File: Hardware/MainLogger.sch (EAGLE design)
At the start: 152 parts, among them J2 GEMS_POWER_PLUGINPUT, J3 CONN_TALON_LOGGER, J4 U.FL, J5 CONN_TALON_LOGGER, J6 CONN_TALON_LOGGER, J8 CONN_TALON_LOGGER, Q1 DMG3404, Q2 MOSFET_PCH-DMP3036SFG, Q3 MOSFET_PCH-DMP3036SFG, Q4 DMG3404, Q5 NX2301P, U1 MMC5633, U10 MXC6655, U11 FXMAR2102UMLP, U12 MCP79412SOIC, U13 SN74LVC1G17DCK, U14 TPL5010DDC, U15 MIC842L, U16 TPL5010DDC, U17 TPL5010DDC, U18 HALL_EFFECT_SI7201, U19 LP59073.3VYKE, U2 PAC1934QFN, U21 MIC22602, U3 LTC4412S6, U4 BQ25616, U5 TPS78218DBV, U6 MAX-M8W, U7 B_SERIES_M.2EKEY_3042, U8 TCR2LE31ESV, U9 TPS61282D

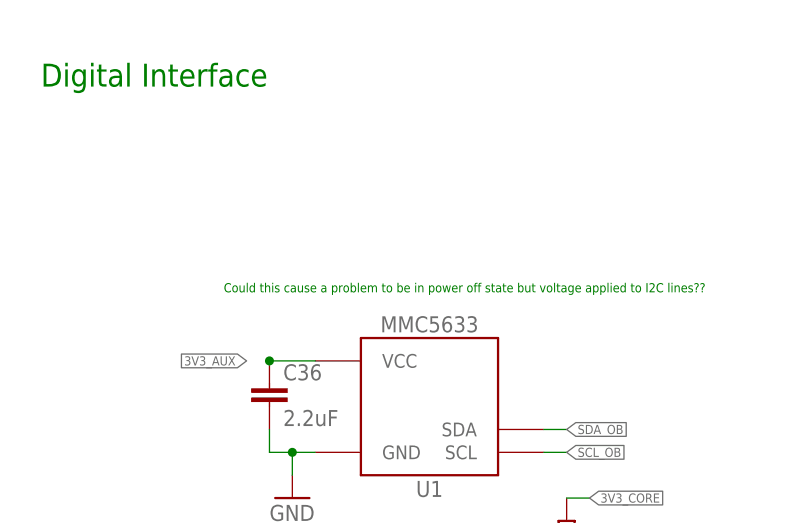
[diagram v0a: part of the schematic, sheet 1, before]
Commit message: Added VELM3328
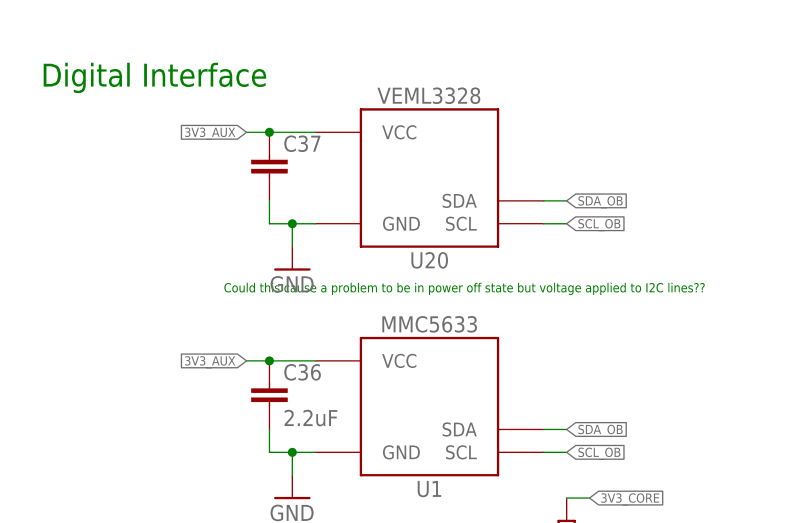
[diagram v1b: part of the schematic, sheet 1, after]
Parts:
- added C37: (no value), bschulz_passives:C-EU0.1UFC0402
- added U20: VEML3328, bschulz:VEML3328
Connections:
- net 3V3_AUX: now also C37.1, U20.VCC
- net GND: now also C37.2, U20.GND
- net SCL_OB: now also U20.SCL
- net SDA_OB: now also U20.SDA
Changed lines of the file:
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@@
 <part name="C36" library="bschulz_passives" deviceset="C-EU" device="C0603" technology="2.2UF" value="2.2uF"/>
 <part name="R6" library="bschulz_passives" deviceset="R-EU_" device="R0402" technology="10K" value="10k"/>
+<part name="U20" library="bschulz" deviceset="VEML3328" device=""/>
+<part name="GND41" library="supply1" library_urn="urn:adsk.eagle:library:371" deviceset="GND" device=""/>
+<part name="C37" library="bschulz_passives" deviceset="C-EU" device="C0402" technology="0.1UF"/>
 </parts>
 <sheets>
@@
 <attribute name="VALUE" x="69.342" y="148.59" size="1.778" layer="96" rot="R90"/>
 </instance>
+<instance part="U20" gate="G$1" x="50.8" y="193.04" smashed="yes">
+<attribute name="DISP" x="50.8" y="202.184" size="1.778" layer="95" ratio="15" align="center"/>
+<attribute name="NAME" x="50.8" y="183.896" size="1.778" layer="95" ratio="15" align="center"/>
+</instance>
+<instance part="GND41" gate="1" x="35.56" y="182.88" smashed="yes">
+<attribute name="VALUE" x="33.02" y="180.34" size="1.778" layer="96"/>
+</instance>
+<instance part="C37" gate="G$1" x="33.02" y="195.58" smashed="yes">
+<attribute name="NAME" x="34.544" y="195.961" size="1.778" layer="95"/>
+<attribute name="VALUE" x="34.544" y="190.881" size="1.778" layer="96"/>
+</instance>
 </instances>
 <busses>
@@
 <wire x1="33.02" y1="137.16" x2="35.56" y2="137.16" width="0.1524" layer="91"/>
 <junction x="35.56" y="137.16"/>
+</segment>
+<segment>
+<pinref part="U20" gate="G$1" pin="GND"/>
+<wire x1="38.1" y1="187.96" x2="35.56" y2="187.96" width="0.1524" layer="91"/>
+<wire x1="35.56" y1="187.96" x2="35.56" y2="185.42" width="0.1524" layer="91"/>
+<pinref part="GND41" gate="1" pin="GND"/>
+<pinref part="C37" gate="G$1" pin="2"/>
+<wire x1="33.02" y1="190.5" x2="33.02" y2="187.96" width="0.1524" layer="91"/>
+<wire x1="33.02" y1="187.96" x2="35.56" y2="187.96" width="0.1524" layer="91"/>
+<junction x="35.56" y="187.96"/>
 </segment>
 </net>
@@
 <label x="63.5" y="119.38" size="1.016" layer="95" xref="yes"/>
 </segment>
+<segment>
+<pinref part="U20" gate="G$1" pin="SDA"/>
+<wire x1="63.5" y1="190.5" x2="66.04" y2="190.5" width="0.1524" layer="91"/>
+<label x="66.04" y="190.5" size="1.016" layer="95" xref="yes"/>
+</segment>
 </net>
 <net name="SCL_OB" class="0">
@@
 <wire x1="63.5" y1="116.84" x2="60.96" y2="116.84" width="0.1524" layer="91"/>
 <label x="63.5" y="116.84" size="1.016" layer="95" xref="yes"/>
+</segment>
+<segment>
+<pinref part="U20" gate="G$1" pin="SCL"/>
+<wire x1="63.5" y1="187.96" x2="66.04" y2="187.96" width="0.1524" layer="91"/>
+<label x="66.04" y="187.96" size="1.016" layer="95" xref="yes"/>
 </segment>
 </net>
@@
 <pinref part="C36" gate="G$1" pin="1"/>
 <junction x="33.02" y="172.72"/>
-</segment>
-</net>
+<wire x1="33.02" y1="172.72" x2="30.48" y2="172.72" width="0.1524" layer="91"/>
+</segment>
+<segment>
+<pinref part="U20" gate="G$1" pin="VCC"/>
+<wire x1="38.1" y1="198.12" x2="33.02" y2="198.12" width="0.1524" layer="91"/>
+<pinref part="C37" gate="G$1" pin="1"/>
+<wire x1="33.02" y1="198.12" x2="30.48" y2="198.12" width="0.1524" layer="91"/>
+<junction x="33.02" y="198.12"/>
+<label x="30.48" y="198.12" size="1.016" layer="95" rot="R180" xref="yes"/>
+</segment>
+</net>

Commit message: Continued layout and schematic updates
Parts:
- removed C12: 1uF, bschulz_passives:C-EU1UFC0603
- removed C22, C30, C31: 0.1uF, bschulz_passives:C-EU0.1UFC0402
- removed C29: 10uF, bschulz_passives:C-EU10UFC0805
- removed D7: LEDRED0603, bschulz:LEDRED0603
- removed D8: LEDGREEN0603, bschulz:LEDGREEN0603
- removed FB6: (no value), bschulz:FERRITE_BEAD1KS0402
- removed J3, J5, J6, J8: CONN_TALON_LOGGER, GEMS_Plugs:CONN_TALON_LOGGER
- removed J7: (no value), bschulz:CONN_02-JST-2MM-SMT
- removed R2, R39, R4, R40, R41, R49: 10k, bschulz_passives:R-EU_10KR0402
- removed R22: 100k, bschulz_passives:R-EU_100KR0402
- removed R35: 1k, bschulz_passives:R-EU_1KR0402
- removed R36: 1k, bschulz_passives:R-EU_1KR0603
- removed R42, R43: 4.7k, bschulz_passives:R-EU_4.7KR0603
- removed S1: SP3TCS-4-13NA, bschulz:SP3TCS-4-13NA
- added C38, C41, C42, C43, C54: 0.1uF, bschulz_passives:C-EU0.1UFC0402
- added C39: 1uF, bschulz_passives:C-EU1UFC0603
- added C40: 0.1uF, bschulz_passives:C-EU0.1UFC0603
- added D1: CLVBA-FKA, bschulz:CLVBA-FKA
- added D10, D12, D13, D14, D15, D16, D17: LED0603, bschulz:LED0603
- added FB3: (no value), bschulz:FERRITE_BEAD1KS0402
- added H1, H2, H3, H4: (no value), bschulz:MOUNTING_HOLE4_NP
- added J9: (no value), bschulz:CONN_02-JST-2MM-SMT
- added R10, R52: 10k, bschulz_passives:R-EU_10KR0402
- added R51, R71, R72, R73, R74, R75, R76: 220R, bschulz_passives:R-EU_220R0603
- added R54: 100k, bschulz_passives:R-EU_100KR0603
- added R60: 0R, bschulz_passives:R-EU_0.0R0402
- added R63, R64, R65: 2m, bschulz_passives:R-EU_0.002R0805
- added R66: 10m, bschulz_passives:R-EU_0.01R0805
- added R67, R68, R69, R70: (no value), bschulz_passives:R-EU_R0603
- added R7, R8, R9: 4.7k, bschulz_passives:R-EU_4.7KR0603
- added S3, S4: BUTTON4.2X3.2, bschulz:BUTTON4.2X3.2
- added SD2: MICROSDMOLEX_503182, bschulz:MICROSDMOLEX_503182
- added U23: MB85RC, bschulz:MB85RC
- added U24: SN74AUP3G34DCU, bschulz:SN74AUP3G34DCU
- added U25: SIP32431TDFN, bschulz:SIP32431TDFN
- added U26: PAC1934QFN, bschulz:PAC1934QFN
- added U27: MCP23018QFN, bschulz:MCP23018QFN
- added U28: PCA9634QFN, bschulz:PCA9634QFN
- C11: value 1uF -> 0.1uF; device bschulz_passives:C-EU1UFC0603 -> bschulz_passives:C-EU0.1UFC0402
- C23, C24: value 6pF -> 9pF; device bschulz_passives:C-EU6PFC0402 -> bschulz_passives:C-EU9PFC0402
- C37: value (none) -> 0.1uF
- D5: value (none) -> LED0603; device bschulz:DIODE_CCBAT54CSOT23 -> bschulz:LED0603
- R1, R23, R3: value 100k -> 1M; device bschulz_passives:R-EU_100KR0402 -> bschulz_passives:R-EU_1MR0402
- R20: value 0R -> 100k; device bschulz_passives:R-EU_0.0R0402 -> bschulz_passives:R-EU_100KR0603
- R32: value 10k -> 100k; device bschulz_passives:R-EU_10KR0402 -> bschulz_passives:R-EU_100KR0402
- R33: value 10k -> 220R; device bschulz_passives:R-EU_10KR0402 -> bschulz_passives:R-EU_220R0603
- U14: value TPL5010DDC -> FXMAR2102UMLP; device bschulz:TPL5010DDC -> bschulz:FXMAR2102UMLP
- U15: value MIC842L -> SN74AUP1G08DCK; device bschulz:MIC842L -> bschulz:SN74AUP1G08DCK
- U5: value TPS78218DBV -> MCP23018QFN; device bschulz:TPS78218DBV -> bschulz:MCP23018QFN
- XTAL1: value CRYSTAL3.2X1.5 -> CRYSTAL32.768KHZ_9PF3.2X1.5; device bschulz:CRYSTAL3.2X1.5 -> bschulz:CRYSTAL32.768KHZ_9PF3.2X1.5
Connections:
- removed net !PG: D4.CATHODE, R29.1, R35.2, U4.!PG
- removed net 3V3_EXT_FAULT: D7.CATHODE
- removed net ALERT: R3.1, U2.SLOW/!ALERT
- removed net BYPASS: U9.!BYP
- removed net N$11: R22.1, S1.J3
- removed net N$14: R40.2, U14.DELAY
- removed net N$16: C29.1, R41.2, U15.INP
- removed net N$19: R39.1, R41.1, U14.RSTN
- removed net N$26: R42.2, R43.2, U15.OUT
- removed net N$27: D7.ANODE, R42.1
- removed net N$28: D8.ANODE, R43.1
- removed net N$31: R35.1
- removed net N$34: R36.1
- removed net N$8: R21.1, S1.J2
- removed net N$9: R20.1, S1.J1
- removed net PG: R55.1, U21.POR/PG, U9.PG
- removed net ST: Q4.D, R23.1
- removed net STAT: D3.CATHODE, R26.1, R36.2, U4.STAT
- removed net TIMEPULSE: FB6.2, U6.TIMEPULSE
- removed net TIMEPULSE_EXT: FB6.1
- removed net VBAT: C20.1, C21.+, L2.1, U9.VIN
- removed net VLOGIC: C2.1, C3.1, D5.C, R1.2, R23.2, R3.2, U2.VDD, U2.VDD_IO
- removed net VLOGIC_BUS: D5.A2, J2.3V3, R2.2, R4.2
- removed net VOUT: C18.1, C19.1, U9.VOUT
- removed net V_BACKUP: C14.1, U6.V_BCKP
- new net !CHG_PG: D4.CATHODE, R29.1, U27.GPA3, U4.!PG
- new net !TALON1_FAULT: U5.GPB4
- new net !TALON2_FAULT: U5.GPB5
- new net !TALON3_FAULT: U5.GPB6
- new net !TALON4_FAULT: U5.GPB7
- new net 3V3_AUX_PG: R55.1, U21.POR/PG, U27.GPA0
- new net 3V3_BULK: R65.1, U26.SENSE4-
- new net 3V3_BULK+: C44.1, C46.+, L3.2, R55.2, R56.2, R64.2, R65.2, U26.SENSE3+, U26.SENSE4+
- new net 3V3_CORE+: C34.1, R66.1, U19.VOUT, U26.SENSE2+
- new net 3V3_SD: C40.1, R20.2, U24.VCC, U25.VOUT
- new net 3V3_SD_EN: R54.2, U25.EN, U27.GPB4
- new net CHG_SOURCE: Q4.D, R23.1, U27.GPA5
- new net CHG_STAT: D3.CATHODE, R26.1, U27.GPA4, U4.STAT
- new net CSA_ALERT: R3.1, U2.SLOW/!ALERT, U26.SLOW/!ALERT, U27.GPA2
- new net I2C_EN_GLOBAL: U1.A, U15.A
- new net I2C_EN_LOCAL: U1.Y, U10.EN
- new net I2C_EXT_EN: U15.B, U27.GPB2
- new net I2C_EXT_EN_OUT: U14.EN, U15.Y
- new net I2C_GLOBAL_EN: U7U1.GPIO1
- new net LED_BLUE: R7.2, U7U1.RGB_BLUE
- new net LED_EN: R32.1, U27.GPB5, U28.!OE, U7U1.ADC7
- new net LED_GREEN: R8.2, U7U1.RGB_GREEN
- new net LED_RED: R9.2, U7U1.RGB_RED
- new net MISO: SD2.DATA_OUT, U7U1.MISO
- new net MOSI: U24.1A, U7U1.MOSI
- new net MOSI_BUF: SD2.DATA_IN, U24.1Y
- new net N$15: R50.1, U27.GPB1
- new net N$21: D1.BLUE_CATH, R7.1
- new net N$22: D1.GREEN_CATH, R8.1
- new net N$23: D1.RED_CATH, R9.1
- new net N$24: FB3.1, U6.RESET_N
- new net N$36: D5.CATHODE, U28.LED0
- new net N$37: D10.CATHODE, U28.LED1
- new net N$38: R67.2, R68.1, U27.ADDR
- new net N$39: D12.CATHODE, U28.LED2
- new net N$40: D13.CATHODE, U28.LED3
- new net N$41: D14.CATHODE, U28.LED4
- new net N$42: D15.CATHODE, U28.LED5
- new net N$43: D16.CATHODE, U28.LED6
- new net N$44: D17.CATHODE, U28.LED7
- new net N$45: D5.ANODE, R33.1
- new net N$46: D10.ANODE, R51.1
- new net N$47: D12.ANODE, R71.1
- new net N$48: D13.ANODE, R72.1
- new net N$49: D14.ANODE, R73.1
- new net N$50: D15.ANODE, R74.1
- new net N$51: D16.ANODE, R75.1
- new net N$52: D17.ANODE, R76.1
- new net OB_INT: U27.INTA, U7U1.ADC5
- new net SCK: U24.2A, U7U1.SCK
- new net SCK_BUF: SD2.SCLK, U24.2Y
- new net SCL_GPS: FB2.2, U6.SCL
- new net SDA_GPS: FB1.2, U6.SDA
- new net SD_CD: R20.1, SD2.CARD_DETECT, U27.GPA7
- new net SD_CS: U24.3A, U7U1.CS
- new net SD_CS_BUF: SD2.CS, U24.3Y
- new net TALON1_EN: U5.GPA4
- new net TALON1_GPIOA: U7U1.ADC0
- new net TALON1_GPIOB: U7U1.PWM0
- new net TALON1_I2C_EN: U5.GPB0
- new net TALON1_SEL: U5.GPA0
- new net TALON2_EN: U5.GPA5
- new net TALON2_GPIOA: U7U1.ADC1
- new net TALON2_GPIOB: U7U1.PWM1
- new net TALON2_I2C_EN: U5.GPB1
- new net TALON2_SEL: U5.GPA1
- new net TALON3_EN: U5.GPA6
- new net TALON3_GPIOA: U7U1.ADC2
- new net TALON3_GPIOB: U7U1.PWM2
- new net TALON3_I2C_EN: U5.GPB2
- new net TALON3_SEL: U5.GPA2
- new net TALON4_EN: U5.GPA7
- new net TALON4_GPIOA: U7U1.ADC3
- new net TALON4_GPIOB: U7U1.PWM3
- new net TALON4_I2C_EN: U5.GPB3
- new net TALON4_SEL: U5.GPA3
- new net TALON_INT: U5.INTA, U7U1.ADC4
- new net VBULK: C33.1, C48.1, C49.1, C50.1, C53.1, R63.1, U19.EN, U19.VIN, U21.PVIN, U21.SVIN, U26.SENSE1-
- new net VBULK+: C18.1, C19.1, R63.2, U26.SENSE1+, U9.VOUT
- new net VBULK_PG: U27.GPA1, U9.PG
- new net VDD: SD2.VDD
- net !CE: now also U27.GPB3
- net !FAULT: no longer R36.1
- net !MODE: now also R10.1, S4.1, S4.2
- net !RESET: now also FB3.2, R52.1, S3.1, S3.2, U27.!RESET, U5.!RESET; no longer R49.1
- net 3V3: now also U1.VCC; no longer C13.1, C15.1, C25.1, C30.1, C31.1, R32.2, R33.2, R36.2, R38.2, R39.2, U12.VCC, U14.VDD, U15.VDD, U6.VCC, U6.VCC_IO
- net 3V3_AUX: now also C13.1, C15.1, C39.1, J2.3V3, R64.1, U25.VIN, U26.SENSE3-, U6.VCC, U6.VCC_IO; no longer C44.1, C46.+, L3.2, R55.2, R56.2
- net 3V3_AUX_EN: now also U27.GPB7
- net 3V3_CORE: now also C11.1, C2.1, C25.1, C3.1, C38.1, C41.1, C42.1, C43.1, C54.1, D1.ANODE, R1.2, R10.2, R23.2, R3.2, R32.2, R33.2, R38.2, R51.2, R52.2, R66.2, R68.2, R70.2, R71.2, R72.2, R73.2, R74.2, R75.2, R76.2, U12.VCC, U14.VA, U14.VB, U15.VCC, U2.VDD, U2.VDD_IO, U23.A0, U23.A1, U23.A2, U23.VDD, U26.SENSE2-, U26.VDD, U26.VDD_IO, U27.VDD, U28.VDD, U5.VDD, U7U1.3V3@10, U7U1.3V3@12; no longer C22.1, C34.1, R49.2, U19.VOUT
- net 3V3_TALON: no longer C22.+
- net ACCEL_INT: now also U27.GPA6
- net BCKP_GPS: now also C14.1, U6.V_BCKP
- net CSA_EN: now also U26.!PWRDN, U27.GPB6
- net D+: now also U7U1.UB_USB_P, U7U1.USB_P
- net D-: now also U7U1.UB_USB_N, U7U1.USB_N
- net EN: no longer U9.EN
- net GND: now also C38.2, C39.2, C40.2, C41.2, C42.2, C43.2, C54.2, R54.1, R60.1, R67.1, R69.1, S3.3, S3.4, S4.3, S4.4, SD2.CARD_DETECT1, SD2.GND, SD2.GND1, SD2.VSS, U23.VSS, U23.WP, U24.GND, U25.GND, U26.GND, U27.VSS, U28.VSS, U5.VSS, U7U1.AGND@39, U7U1.AGND@49, U7U1.GND@1, U7U1.GND@15, U7U1.GND@21, U7U1.GND@3, U7U1.GND@5, U7U1.GND@56, U7U1.GND@7, U7U1.GND@76, U7U1.GND@77, U7U1.GND@9; no longer C12.2, C22.-, C22.2, C29.2, C30.2, C31.2, D8.CATHODE, R20.2, R22.2, R35.1, R40.1, U14.DONE, U5.GND
- net GPS_INT: now also U27.GPB0
- net I2C_EN: now also U1.B; no longer R35.2, U10.EN
- net I2C_OB_EN: now also U7U1.ADC6
- net N$17: now also R60.2, U26.ADDR_SEL; no longer C12.1, D5.A1, U5.VOUT
- net N$35: now also R69.2, R70.1, U5.ADDR; no longer R50.1
- net RTC_INT: now also U7U1.GPIO0
- net RX: now also U7U1.RX; no longer U6.RXD
- net SCL: now also U14.A2, U7U1.SCL; no longer FB2.2, J2.SCL, R2.1, U12.SCL, U2.CLK, U6.SCL
- net SCL_EXT: now also J2.SCL, U14.B2; no longer FB2.1, R33.1
- net SCL_OB: now also FB2.1, U12.SCL, U2.CLK, U23.SCL, U26.CLK, U27.SCL, U28.SCL, U5.SCL
- net SDA: now also U14.A1, U7U1.SDA; no longer FB1.2, J2.SDA, R4.1, U2.DATA, U6.SDA
- net SDA_EXT: now also J2.SDA, U14.B1; no longer FB1.1, R32.1
- net SDA_OB: now also FB1.1, U2.DATA, U23.SDA, U26.DATA, U27.SDA, U28.SDA, U5.SDA
- net SEL: no longer U9.VSEL
- net SYS: now also C20.1, C21.+, L2.1, U7U1.VCC@2, U7U1.VCC@4, U7U1.VCC@6, U7U1.VCC@8, U9.!BYP, U9.EN, U9.VIN, U9.VSEL; no longer C11.1, C33.1, C48.1, C49.1, C50.1, C53.1, U19.EN, U19.VIN, U21.PVIN, U21.SVIN, U5.EN, U5.VIN
- net TEST: now also U7U1.CTS
- net TX: now also U7U1.TX; no longer U6.TXD
- net VSET: now also R21.1; no longer S1.C
- net VUSB: now also U7U1.UB_VBUS, U7U1.VBUS
- net WDT_DONE: now also U7U1.RTS
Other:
- note added: "Cell"
- note added: "Change to load switch with lower limit and/or fault status indication??"
- note added: "Connect Ax HIGH to avoid conflict with external EEPROMs"
- note added: "D2"
- note added: "D3"
- note added: "FLEX"
- note added: "GPS"
- note added: "High normal Low when using USB"
- note added: "On Board Interface"
- note added: "Other"
- note added: "Particle uses 1k on eval board Test 4.7k (or more) for reduced power consumption"
- note added: "Select address!"
- note added: "Sensor"
- note added: "Should this be 3V3_AUX?"
- note added: "Should this be used?"
- note added: "Talon Interface"
- note added: "Use IO Expander push/pull/pullup instead for CSA_EN?"
- note added: "Verify!"
- note added: "uBlox Data Port"
- note removed: "IO Pins: - TEST - WDT_DONE - 3V3_EXT_FAULT - RTC_INT - GPS_INT - VUSB - CSA_EN - ALERT - ST - !CE - STAT - !PG"
- note removed: "Is this the right power rail??"
- note removed: "Remove! Connect to normal logic rails"

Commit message: Initial copper layout complete, cleanup and silk required
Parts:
- C40: device bschulz_passives:C-EU0.1UFC0603 -> bschulz_passives:C-EU0.1UFC0402
- R20, R54: device bschulz_passives:R-EU_100KR0603 -> bschulz_passives:R-EU_100KR0402
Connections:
- removed net VDD: SD2.VDD
- net !TALON1_FAULT: now also U5.GPA2; no longer U5.GPB4
- net !TALON2_FAULT: now also U5.GPA6; no longer U5.GPB5
- net !TALON3_FAULT: now also U5.GPB2; no longer U5.GPB6
- net !TALON4_FAULT: now also U5.GPB6; no longer U5.GPB7
- net 3V3: no longer U10.VA
- net 3V3_CORE: now also U28.A4, U28.A6
- net 3V3_SD: now also SD2.VDD
- net 3V3_TALON: now also U10.VA
- net GND: now also J9.2, U28.A0, U28.A1, U28.A2, U28.A3, U28.A5
- net I2C_EN_GLOBAL: no longer U15.A
- net I2C_GLOBAL_EN: now also U15.A
- net LED_EN: no longer U7U1.ADC7
- net SOLAR+: now also J9.1
- net TALON1_EN: now also U5.GPA3; no longer U5.GPA4
- net TALON1_GPIOA: now also U7U1.ADC3; no longer U7U1.ADC0
- net TALON1_GPIOB: now also U7U1.PWM3; no longer U7U1.PWM0
- net TALON1_I2C_EN: now also U5.GPA1; no longer U5.GPB0
- net TALON2_EN: now also U5.GPA7; no longer U5.GPA5
- net TALON2_GPIOA: now also U7U1.ADC2; no longer U7U1.ADC1
- net TALON2_GPIOB: now also U7U1.PWM2; no longer U7U1.PWM1
- net TALON2_I2C_EN: now also U5.GPA5; no longer U5.GPB1
- net TALON2_SEL: now also U5.GPA4; no longer U5.GPA1
- net TALON3_EN: now also U5.GPB3; no longer U5.GPA6
- net TALON3_GPIOA: now also U7U1.ADC1; no longer U7U1.ADC2
- net TALON3_GPIOB: now also U7U1.PWM1; no longer U7U1.PWM2
- net TALON3_I2C_EN: now also U5.GPB1; no longer U5.GPB2
- net TALON3_SEL: now also U5.GPB0; no longer U5.GPA2
- net TALON4_EN: now also U5.GPB7; no longer U5.GPA7
- net TALON4_GPIOA: now also U7U1.ADC0; no longer U7U1.ADC3
- net TALON4_GPIOB: now also U7U1.PWM0; no longer U7U1.PWM3
- net TALON4_I2C_EN: now also U5.GPB5; no longer U5.GPB3
- net TALON4_SEL: now also U5.GPB4; no longer U5.GPA3
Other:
- note added: "ADR: 0x10"
- note added: "ADR: 0x10 ~ 0x1F"
- note added: "ADR: 0x15"
- note added: "ADR: 0x20 ~ 0x27"
- note added: "ADR: 0x29"
- note added: "ADR: 0x30"
- note added: "ADR: 0x42"
- note added: "ADR: 0x57"
- note added: "Have both sides powered by 3V3_TALON for ease of routing If either side is low, device is in tri-state anyway"

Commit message: Layout and cleanup complete, review required
Also add test points
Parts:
- removed C50: 22uF, bschulz_passives:C-EU22UFC0805
- removed C51: 1nF, bschulz_passives:C-EUC0402
- removed C52: 10nF, bschulz_passives:C-EUC0402
- removed C54: 0.1uF, bschulz_passives:C-EU0.1UFC0402
- removed D16, D17: LED0603, bschulz:LED0603
- removed FB7: 30Ω/1.8A, SparkFun-Coils:FERRITE_BEAD-0603
- removed J9: (no value), bschulz:CONN_02-JST-2MM-SMT
- removed R63, R64, R65: 2m, bschulz_passives:R-EU_0.002R0805
- removed R66: 10m, bschulz_passives:R-EU_0.01R0805
- removed R67: (no value), bschulz_passives:R-EU_R0603
- removed R71, R72, R73, R74: 220R, bschulz_passives:R-EU_220R0603
- removed S4: BUTTON4.2X3.2, bschulz:BUTTON4.2X3.2
- removed U27: MCP23018QFN, bschulz:MCP23018QFN
- added $3_178_$_2021-10-08_21-38-43: B_SERIES_M.2EKEY_3042, Particle-Devices:B_SERIES_M.2EKEY_3042
- added C22: 10uF, bschulz_passives:C-EU10UFC0805
- added C29: 220uF, bschulz_passives:CTANT_EU2917
- added C30: 1.5uF, bschulz_passives:C-EU1.5UFC0805
- added C31: 47nF, bschulz_passives:C-EUC0603
- added D7: BAT54WS, bschulz:DIODE_SCHOTTKYSOD-323
- added D8: LED0603, bschulz:LED0603
- added FB4: (no value), bschulz:FERRITE_BEAD1KS0402
- added J3: GEMS_POWER_PLUGINPUT, bschulz:GEMS_POWER_PLUGINPUT
- added R2, R49: 1M, bschulz_passives:R-EU_1MR0402
- added R22, R4: 0R, bschulz_passives:R-EU_0.0R0402
- added R35, R41, R42: 10k, bschulz_passives:R-EU_10KR0402
- added R43, R53: 100k, bschulz_passives:R-EU_100KR0402
- added S1: BUTTON4.2X3.2, bschulz:BUTTON4.2X3.2
- C10: value 10uF -> 1uF; device bschulz_passives:C-EU10UFC0805 -> bschulz_passives:C-EU1UFC0603
- C14: value 0.1uF -> 1uF; device bschulz_passives:C-EU0.1UFC0402 -> bschulz_passives:C-EU1UFC0603
- C15: value 1uF -> 22uF; device bschulz_passives:C-EU1UFC0603 -> bschulz_passives:C-EU22UFC0805
- C16, C17: value 0.1uF -> 22uF; device bschulz_passives:C-EU0.1UFC0402 -> bschulz_passives:C-EU22UFC0805
- C18: value 10uF -> 1nF; device bschulz_passives:C-EU10UFC0805 -> bschulz_passives:C-EUC0402
- C19, C5, C6, C9: value 10uF -> 0.1uF; device bschulz_passives:C-EU10UFC0805 -> bschulz_passives:C-EU0.1UFC0402
- C2, C3: value 0.1uF -> 2.2uF; device bschulz_passives:C-EU0.1UFC0402 -> bschulz_passives:C-EU2.2UFC0603
- C20: value 1.5uF -> 10nF; device bschulz_passives:C-EU1.5UFC0805 -> bschulz_passives:C-EUC0402
- C21: value 220uF -> 1uF; device bschulz_passives:CTANT_EU2917 -> bschulz_passives:C-EU1UFC0603
- C23: value 9pF -> 39pF; device bschulz_passives:C-EU9PFC0402 -> bschulz_passives:C-EUC0402
- C24: value 9pF -> 10nF; device bschulz_passives:C-EU9PFC0402 -> bschulz_passives:C-EUC0402
- C25: value 0.1uF -> 100pF; device bschulz_passives:C-EU0.1UFC0402 -> bschulz_passives:C-EUC0402
- C26: value 47pF -> 1uF; device bschulz_passives:C-EUC0402 -> bschulz_passives:C-EU1UFC0603
- C27: value 0.1uF -> 100uF; device bschulz_passives:C-EU0.1UFC0402 -> bschulz_passives:CTANT_EU1411
- C28, C33, C34: value 1uF -> 10uF; device bschulz_passives:C-EU1UFC0603 -> bschulz_passives:C-EU10UFC0805
- C32: value 0.1uF -> 4.7uF; device bschulz_passives:C-EU0.1UFC0402 -> bschulz_passives:C-EU4.7UFC0805
- C35, C36: value 2.2uF -> 10uF; device bschulz_passives:C-EU2.2UFC0603 -> bschulz_passives:C-EU10UFC0805
- C4: value 1uF -> 0.1uF; device bschulz_passives:C-EU1UFC0603 -> bschulz_passives:C-EU0.1UFC0402
- C41: value 0.1uF -> 47pF; device bschulz_passives:C-EU0.1UFC0402 -> bschulz_passives:C-EUC0402
- C43: value 0.1uF -> 9pF; device bschulz_passives:C-EU0.1UFC0402 -> bschulz_passives:C-EU9PFC0402
- C44: value 10nF -> 9pF; device bschulz_passives:C-EUC0402 -> bschulz_passives:C-EU9PFC0402
- C45: value 100pF -> 0.1uF; device bschulz_passives:C-EUC0402 -> bschulz_passives:C-EU0.1UFC0402
- C46: value 100uF -> 1uF; device bschulz_passives:CTANT_EU1411 -> bschulz_passives:C-EU1UFC0603
- C47: value 39pF -> 0.1uF; device bschulz_passives:C-EUC0402 -> bschulz_passives:C-EU0.1UFC0402
- C48, C49: value 22uF -> 0.1uF; device bschulz_passives:C-EU22UFC0805 -> bschulz_passives:C-EU0.1UFC0402
- C7: value 47nF -> 0.1uF; device bschulz_passives:C-EUC0603 -> bschulz_passives:C-EU0.1UFC0402
- C8: value 4.7uF -> 0.1uF; device bschulz_passives:C-EU4.7UFC0805 -> bschulz_passives:C-EU0.1UFC0402
- D1: value CLVBA-FKA -> LED0603; device bschulz:CLVBA-FKA -> bschulz:LED0603
- D11: value CDBA3100 -> LED0603; device bschulz:DIODE_SCHOTTKYDO-214AC -> bschulz:LED0603
- D2: value LED0603 -> CDBA3100; device bschulz:LED0603 -> bschulz:DIODE_SCHOTTKYDO-214AC
- D3: value LED0603 -> BAT54C; device bschulz:LED0603 -> bschulz:DIODE_CCBAT54CSOT23
- D6: value BAT54C -> CLVBA-FKA; device bschulz:DIODE_CCBAT54CSOT23 -> bschulz:CLVBA-FKA
- D9: value BAT54WS -> LED0603; device bschulz:DIODE_SCHOTTKYSOD-323 -> bschulz:LED0603
- FB5: value (none) -> 30Ω/1.8A; device bschulz:FERRITE_BEAD1KS0402 -> SparkFun-Coils:FERRITE_BEAD-0603; DIGIKEY (none) -> 445-2986-1-ND; MF (none) -> TDK; MPN (none) -> MPZ1608D300BTA00
- J1: device bschulz:CONN_023.5MM_ROUND_RESTRICT -> bschulz:CONN_02-JST-2MM-SMT
- J2: value GEMS_POWER_PLUGINPUT -> (none); device bschulz:GEMS_POWER_PLUGINPUT -> bschulz:CONN_023.5MM_ROUND_RESTRICT
- L1: value 1uH -> 1uF
- L3: value 1uF -> 1uH
- R10: value 10k -> 2m; device bschulz_passives:R-EU_10KR0402 -> bschulz_passives:R-EU_R0805
- R11: value 2m -> 1k; device bschulz_passives:R-EU_R0805 -> bschulz_passives:R-EU_1KR0402
- R12: value 1k -> 100k; device bschulz_passives:R-EU_1KR0402 -> bschulz_passives:R-EU_100KR0402
- R13: value 1k -> 100k; device bschulz_passives:R-EU_1KR0603 -> bschulz_passives:R-EU_100KR0402
- R14: value 0R -> 470k; device bschulz_passives:R-EU_0.0R0402 -> bschulz_passives:R-EU_470KR0603
- R15: value 2m -> 10m; device bschulz_passives:R-EU_R0805 -> bschulz_passives:R-EU_0.01R0805
- R16: value 1M -> 1k; device bschulz_passives:R-EU_1MR0402 -> bschulz_passives:R-EU_1KR0603
- R17: value 470R -> 1M; device bschulz_passives:R-EU_R0603 -> bschulz_passives:R-EU_1MR0402
- R18: value 220R -> 20k; device bschulz_passives:R-EU_R0603 -> bschulz_passives:R-EU_R0402
- R19: value 470k -> 100k; device bschulz_passives:R-EU_470KR0603 -> bschulz_passives:R-EU_100KR0402
- R20, R54: value 100k -> 10k; device bschulz_passives:R-EU_100KR0402 -> bschulz_passives:R-EU_10KR0402
- R21: value 10k -> 2.7k; device bschulz_passives:R-EU_10KR0402 -> bschulz_passives:R-EU_R0402
- R23: value 1M -> 2m; device bschulz_passives:R-EU_1MR0402 -> bschulz_passives:R-EU_R0805
- R24, R38: value 100k -> 1M; device bschulz_passives:R-EU_100KR0402 -> bschulz_passives:R-EU_1MR0402
- R25: value 100k -> 470R; device bschulz_passives:R-EU_100KR0402 -> bschulz_passives:R-EU_R0603
- R26: value 1M -> 220R; device bschulz_passives:R-EU_1MR0402 -> bschulz_passives:R-EU_R0603
- R28: value 10m -> 100k; device bschulz_passives:R-EU_0.01R0805 -> bschulz_passives:R-EU_100KR0402
- R29, R50: value 1M -> 100k; device bschulz_passives:R-EU_1MR0402 -> bschulz_passives:R-EU_100KR0402
- R3: value 1M -> 0R; device bschulz_passives:R-EU_1MR0402 -> bschulz_passives:R-EU_0.0R0402
- R30: value 10m -> 1M; device bschulz_passives:R-EU_0.01R0805 -> bschulz_passives:R-EU_1MR0402
- R32: value 100k -> 10m; device bschulz_passives:R-EU_100KR0402 -> bschulz_passives:R-EU_0.01R0805
- R33: value 220R -> 1M; device bschulz_passives:R-EU_220R0603 -> bschulz_passives:R-EU_1MR0402
- R34: value 10 -> 10m; device bschulz_passives:R-EU_R0402 -> bschulz_passives:R-EU_0.01R0805
- R37: value 1M -> (none); device bschulz_passives:R-EU_1MR0402 -> bschulz_passives:R-EU_R0603
- R44: value 10k -> 10; device bschulz_passives:R-EU_10KR0402 -> bschulz_passives:R-EU_R0402
- R45: value 1M -> 4.7k; device bschulz_passives:R-EU_1MR0402 -> bschulz_passives:R-EU_4.7KR0603
- R46, R47: value 100k -> 4.7k; device bschulz_passives:R-EU_100KR0402 -> bschulz_passives:R-EU_4.7KR0603
- R48: value 10k -> 100k; device bschulz_passives:R-EU_10KR0402 -> bschulz_passives:R-EU_100KR0402
- R5: value 0R -> 10k; device bschulz_passives:R-EU_0.0R0402 -> bschulz_passives:R-EU_10KR0402
- R51: value 220R -> 10k; device bschulz_passives:R-EU_220R0603 -> bschulz_passives:R-EU_10KR0402
- R52: value 10k -> 1M; device bschulz_passives:R-EU_10KR0402 -> bschulz_passives:R-EU_1MR0402
- R55, R59: value 100k -> 220R; device bschulz_passives:R-EU_100KR0402 -> bschulz_passives:R-EU_220R0603
- R56: value 10k -> 220R; device bschulz_passives:R-EU_10KR0402 -> bschulz_passives:R-EU_220R0603
- R57: value 2.7k -> 220R; device bschulz_passives:R-EU_R0402 -> bschulz_passives:R-EU_220R0603
- R58: value 20k -> 220R; device bschulz_passives:R-EU_R0402 -> bschulz_passives:R-EU_220R0603
- R6: value 10k -> 2m; device bschulz_passives:R-EU_10KR0402 -> bschulz_passives:R-EU_0.002R0805
- R60: value 0R -> 220R; device bschulz_passives:R-EU_0.0R0402 -> bschulz_passives:R-EU_220R0603
- R7, R8: value 4.7k -> 2m; device bschulz_passives:R-EU_4.7KR0603 -> bschulz_passives:R-EU_0.002R0805
- R9: value 4.7k -> 100k; device bschulz_passives:R-EU_4.7KR0603 -> bschulz_passives:R-EU_100KR0402
- S2: value SPDT7103K2CWA -> BUTTON4.2X3.2; device bschulz:SPDT7103K2CWA -> bschulz:BUTTON4.2X3.2
- S3: value BUTTON4.2X3.2 -> SPDT7103K2CWA; device bschulz:BUTTON4.2X3.2 -> bschulz:SPDT7103K2CWA
- U1: value MMC5633 -> FXMAR2102UMLP; device bschulz:MMC5633 -> bschulz:FXMAR2102UMLP
- U10: value MXC6655 -> SIP32431TDFN; device bschulz:MXC6655 -> bschulz:SIP32431TDFN
- U11: value FXMAR2102UMLP -> LTC4412S6; device bschulz:FXMAR2102UMLP -> bschulz:LTC4412S6
- U12: value MCP79412SOIC -> TCR2LE31ESV; device bschulz:MCP79412SOIC -> bschulz:TCR2LE31ESV
- U13: value SN74LVC1G17DCK -> LP59073.3VYKE; device bschulz:SN74LVC1G17DCK -> bschulz:LP59073.3VYKE
- U14: value FXMAR2102UMLP -> MIC22602; device bschulz:FXMAR2102UMLP -> bschulz:MIC22602
- U15: value SN74AUP1G08DCK -> BQ25616; device bschulz:SN74AUP1G08DCK -> bschulz:BQ25616
- U16: value TPL5010DDC -> TPS61282D; device bschulz:TPL5010DDC -> bschulz:TPS61282D
- U17: value TPL5010DDC -> MCP23018QFN; device bschulz:TPL5010DDC -> bschulz:MCP23018QFN
- U18: value HALL_EFFECT_SI7201 -> MCP23018QFN; device bschulz:HALL_EFFECT_SI7201 -> bschulz:MCP23018QFN
- U19: value LP59073.3VYKE -> MAX-M8W; device bschulz:LP59073.3VYKE -> bschulz:MAX-M8W
- U2: value PAC1934QFN -> VEML3328; device bschulz:PAC1934QFN -> bschulz:VEML3328
- U20: value VEML3328 -> MCP79412SOIC; device bschulz:VEML3328 -> bschulz:MCP79412SOIC
- U21: value MIC22602 -> HALL_EFFECT_SI7201; device bschulz:MIC22602 -> bschulz:HALL_EFFECT_SI7201
- U23: value MB85RC -> SN74LVC1G17DCK; device bschulz:MB85RC -> bschulz:SN74LVC1G17DCK
- U24: value SN74AUP3G34DCU -> TPL5010DDC; device bschulz:SN74AUP3G34DCU -> bschulz:TPL5010DDC
- U25: value SIP32431TDFN -> TPL5010DDC; device bschulz:SIP32431TDFN -> bschulz:TPL5010DDC
- U26: value PAC1934QFN -> MB85RC; device bschulz:PAC1934QFN -> bschulz:MB85RC
- U3: value LTC4412S6 -> MMC5633; device bschulz:LTC4412S6 -> bschulz:MMC5633
- U4: value BQ25616 -> MXC6655; device bschulz:BQ25616 -> bschulz:MXC6655
- U5: value MCP23018QFN -> PAC1934QFN; device bschulz:MCP23018QFN -> bschulz:PAC1934QFN
- U6: value MAX-M8W -> PAC1934QFN; device bschulz:MAX-M8W -> bschulz:PAC1934QFN
- U7: value B_SERIES_M.2EKEY_3042 -> SN74AUP1G08DCK; device Particle-Devices:B_SERIES_M.2EKEY_3042 -> bschulz:SN74AUP1G08DCK
- U8: value TCR2LE31ESV -> FXMAR2102UMLP; device bschulz:TCR2LE31ESV -> bschulz:FXMAR2102UMLP
- U9: value TPS61282D -> SN74AUP3G34DCU; device bschulz:TPS61282D -> bschulz:SN74AUP3G34DCU
- renumbered C53 to C12, R68 to R36, R69 to R40, R70 to R39, R75 to R61, R76 to R62, SD2 to SD1, U28 to U22
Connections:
- removed net N$20 (its old number): D3.ANODE, R27.1
- new net N$18: D5.ANODE, R35.1
- net !CE: now also R22.1, U17.GPB3; no longer R14.1, U27.GPB3
- net !CHG_PG: now also D5.CATHODE, R33.1, U15.!PG, U17.GPA3; no longer D4.CATHODE, R29.1, U27.GPA3, U4.!PG
- net !FAULT: now also R1.1, U4.!FAULT; no longer U11.!FAULT
- net !MODE: now also $3_178_$_2021-10-08_21-38-43U1.MODE, C46.1, R42.1, S2.1, S2.2, U21.OUT; no longer C28.1, R10.1, S4.1, S4.2, U18.OUT, U7U1.MODE
- net !RESET: now also $3_178_$_2021-10-08_21-38-43U1.RESET, FB4.2, R41.1, S1.1, S1.2, U17.!RESET, U18.!RESET, U25.RSTN; no longer FB3.2, R52.1, S3.1, S3.2, U17.RSTN, U27.!RESET, U5.!RESET, U7U1.RESET
- net !TALON1_FAULT: now also U18.GPA2; no longer U5.GPA2
- net !TALON2_FAULT: now also U18.GPA6; no longer U5.GPA6
- net !TALON3_FAULT: now also U18.GPB2; no longer U5.GPB2
- net !TALON4_FAULT: now also U18.GPB6; no longer U5.GPB6
- net 3V3: now also C1.1, C2.1, R1.2, U4.VIN; no longer C18.1, C20.1, U11.VIN
- net 3V3_AUX: now also C1.1, C10.1, C2.1, C40.1, J3.3V3, R7.1, U10.VIN, U19.VCC, U19.VCC_IO, U2.VCC, U3.VCC, U6.SENSE3-; no longer C13.1, C15.1, C36.1, C37.1, J2.3V3, R64.1, U1.VCC, U20.VCC, U25.VIN, U26.SENSE3-, U6.VCC, U6.VCC_IO
- net 3V3_AUX_EN: now also R13.1, U14.EN/DLY, U17.GPB7; no longer R59.1, U21.EN/DLY, U27.GPB7
- net 3V3_AUX_PG: now also R19.1, U14.POR/PG, U17.GPA0; no longer R55.1, U21.POR/PG, U27.GPA0
- net 3V3_BULK: now also R8.1, U6.SENSE4-; no longer R65.1, U26.SENSE4-
- net 3V3_BULK+: now also C24.1, C27.+, L1.2, R19.2, R20.2, R7.2, R8.2, U6.SENSE3+, U6.SENSE4+; no longer C44.1, C46.+, L3.2, R55.2, R56.2, R64.2, R65.2, U26.SENSE3+, U26.SENSE4+
- net 3V3_CORE: now also $3_178_$_2021-10-08_21-38-43U1.3V3@10, $3_178_$_2021-10-08_21-38-43U1.3V3@12, C37.1, C4.1, C45.1, C47.1, C49.1, C5.1, C6.1, C7.1, C8.1, C9.1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; no longer C1.1, C11.1, C2.1, C25.1, C32.1, C35.1, C41.1, C42.1, C43.1, C54.1, D1.ANODE, R10.2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
- net 3V3_CORE+: now also C21.1, R15.1, U13.VOUT, U6.SENSE2+; no longer C34.1, R66.1, U19.VOUT, U26.SENSE2+
- net 3V3_SD: now also C11.1, R9.2, U10.VOUT, U9.VCC; no longer C40.1, R20.2, U24.VCC, U25.VOUT
- net 3V3_SD_EN: now also R12.2, U10.EN, U17.GPB4; no longer R54.2, U25.EN, U27.GPB4
- net 3V3_TALON: now also C3.1, C4.+, C5.1, U2.VA, U2.VB, U3.VCC, U4.VOUT; no longer C19.1, C21.1, U10.VA, U10.VB, U11.VOUT, U9.VCC
- net ACCEL_INT: now also R5.1, U17.GPA6, U4.INT; no longer R6.1, U10.INT, U27.GPA6
- net ANT_VCC: now also C41.1, FB5.2, R44.1; no longer C26.1, FB7.2, R34.1
- net BAT: now also J3.BAT, R32.2, U5.SENSE1-; no longer J2.BAT, R28.2, U2.SENSE1-
- net BAT_CHG: now also C33.1, C48.1, D3.A2, R32.1, S3.P, U15.BAT, U24.VDD, U5.SENSE1+; no longer C27.1, C9.1, D6.A2, R28.1, S2.P, U16.VDD, U2.SENSE1+, U4.BAT
- net BCKP_GPS: now also C42.1, D3.A1, R16.2, U19.V_BCKP; no longer C14.1, D6.A1, R13.2, U6.V_BCKP
- net BCKP_RTC: now also D3.C, U20.VBAT; no longer D6.C, U12.VBAT
- net BTST: now also C31.2, U15.BTST; no longer C7.2, U4.BTST
- net CHG_SOURCE: now also R17.1, U17.GPA5; no longer R23.1, U27.GPA5
- net CHG_STAT: now also D4.CATHODE, R30.1, U15.STAT, U17.GPA4; no longer D3.CATHODE, R26.1, U27.GPA4, U4.STAT
- net COMP: now also C23.1, U14.COMP; no longer C47.1, U21.COMP
- net CSA_ALERT: now also R2.1, U17.GPA2, U5.SLOW/!ALERT, U6.SLOW/!ALERT; no longer R3.1, U2.SLOW/!ALERT, U26.SLOW/!ALERT, U27.GPA2
- net CSA_EN: now also U17.GPB6, U5.!PWRDN, U6.!PWRDN; no longer U2.!PWRDN, U26.!PWRDN, U27.GPB6
- net D+: now also $3_178_$_2021-10-08_21-38-43U1.UB_USB_P, $3_178_$_2021-10-08_21-38-43U1.USB_P, U15.D+; no longer U4.D+, U7U1.UB_USB_P, U7U1.USB_P
- net D-: now also $3_178_$_2021-10-08_21-38-43U1.UB_USB_N, $3_178_$_2021-10-08_21-38-43U1.USB_N, U15.D-; no longer U4.D-, U7U1.UB_USB_N, U7U1.USB_N
- net DELAY: now also C20.1, U14.DELAY; no longer C52.1, U21.DELAY
- net EN: now also U4.EN; no longer U11.EN
- net EN_MAIN: now also R51.2, U24.RSTN; no longer R44.2, U16.RSTN
- net FAULT_BUS: now also D1.ANODE, R11.2; no longer D2.ANODE, R12.2
- net FB: now also C24.2, C25.1, R20.1, R21.2, U14.FB; no longer C44.2, C45.1, R56.1, R57.2, U21.FB
- net GND: now also $3_178_$_2021-10-08_21-38-43U1.AGND@39, $3_178_$_2021-10-08_21-38-43U1.AGND@49, $3_178_$_2021-10-08_21-38-43U1.GND@1, $3_178_$_2021-10-08_21-38-43U1.GND@15, $3_178_$_2021-10-08_21-38-43U1.GND@21, $3_178_$_2021-10-08_21-38-43U1.GND@3, $3_178_$_2021-10-08_21-38-43U1.GND@5, $3_178_$_2021-10-08_21-38-43U1.GND@56, $3_178_$_2021-10-08_21-38-43U1.GND@7, $3_178_$_2021-10-08_21-38-43U1.GND@76, $3_178_$_2021-10-08_21-38-43U1.GND@77, $3_178_$_2021-10-08_21-38-43U1.GND@9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; no longer C21.-, C23.2, C24.2, C27.2, C46.-, C50.2, C51.2, C52.2, C54.2, D11.A, D2.CATHODE, J2.GND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
- net GPIOA: now also U3.1B1; no longer U9.1B1
- net GPIOB: now also U3.2B1; no longer U9.2B1
- net GPS_ANT: now also FB5.1, U19.RF_IN; no longer FB7.1, U6.RF_IN
- net GPS_INT: now also FB3.1, U17.GPB0; no longer FB5.1, U27.GPB0
- net GPS_INT_CLEAN: now also FB3.2, U19.EXTINT; no longer FB5.2, U6.EXTINT
- net I2C_EN_LOCAL: now also U2.EN; no longer U10.EN
- net I2C_EXT_EN: now also U17.GPB2, U7.B; no longer U15.B, U27.GPB2
- net I2C_EXT_EN_OUT: now also U7.Y, U8.EN; no longer U14.EN, U15.Y
- net I2C_GLOBAL_EN: now also $3_178_$_2021-10-08_21-38-43U1.GPIO1, U7.A; no longer U15.A, U7U1.GPIO1
- net I2C_OB_EN: now also $3_178_$_2021-10-08_21-38-43U1.ADC6, U1.EN; no longer U11.EN, U7U1.ADC6
- net ICHG: now also R26.2, U15.ICHG; no longer R18.2, U4.ICHG
- net ILIM: now also R25.2, U15.ILIM; no longer R17.2, U4.ILIM
- net LED_BLUE: now also $3_178_$_2021-10-08_21-38-43U1.RGB_BLUE, R47.2; no longer R7.2, U7U1.RGB_BLUE
- net LED_EN: now also R53.1, U17.GPB5; no longer R32.1, U27.GPB5
- net LED_GREEN: now also $3_178_$_2021-10-08_21-38-43U1.RGB_GREEN, R46.2; no longer R8.2, U7U1.RGB_GREEN
- net LED_RED: now also $3_178_$_2021-10-08_21-38-43U1.RGB_RED, R45.2; no longer R9.2, U7U1.RGB_RED
- net MISO: now also $3_178_$_2021-10-08_21-38-43U1.MISO; no longer U7U1.MISO
- net MOSI: now also $3_178_$_2021-10-08_21-38-43U1.MOSI, U9.1A; no longer U24.1A, U7U1.MOSI
- net MOSI_BUF: now also U9.1Y; no longer U24.1Y
- net N$1: now also R3.2, U5.ADDR_SEL; no longer R5.2, U2.ADDR_SEL
- net N$10: now also R22.2, R24.2, U15.!CE; no longer R14.2, R16.2, U4.!CE
- net N$12: now also D7.A, R49.2, S3.S, U23.A; no longer D9.A, R45.2, S2.S, U13.A
- net N$13: now also C46.2, R48.1; no longer C28.2, R47.1
- net N$15: now also R38.1, U17.GPB1; no longer R50.1, U27.GPB1
- net N$17: now also R4.2, U6.ADDR_SEL; no longer R60.2, U26.ADDR_SEL
- net N$21: now also D6.BLUE_CATH, R47.1; no longer D1.BLUE_CATH, R7.1
- net N$22: now also D6.GREEN_CATH, R46.1; no longer D1.GREEN_CATH, R8.1
- net N$23: now also D6.RED_CATH, R45.1; no longer D1.RED_CATH, R9.1
- net N$24: now also FB4.1, U19.RESET_N; no longer FB3.1, U6.RESET_N
- net N$25: now also J3.FAULT, R11.1; no longer J2.FAULT, R12.1
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
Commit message: Layout, gerbers, and BoM for v0.0 - sent to fab
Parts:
- added D16: RCLAMP3654, bschulz:RCLAMP3654
- added R63, R64: 27R, bschulz_passives:R-EU_27R0402
- added TP1, TP2, TP3, TP4, TP5, TP6, TP7, TP8, TP9: TESTPOINTRCU, bschulz:TESTPOINTRCU
- C18: device bschulz_passives:C-EUC0402 -> bschulz_passives:C-EU1NFC0402
- C20, C24: device bschulz_passives:C-EUC0402 -> bschulz_passives:C-EU10NFC0402
- C23: device bschulz_passives:C-EUC0402 -> bschulz_passives:C-EU39PFC0402
- C25: device bschulz_passives:C-EUC0402 -> bschulz_passives:C-EU100PFC0402
- C27: DIGIKEY (none) -> 478-5231-1-ND; MF (none) -> Kyocera AVX; MPN (none) -> TPSB107M010R0400
- C29: DIGIKEY (none) -> 399-9744-1-ND; MF (none) -> Kemet; MPN (none) -> T491D227M010AT
- C31: device bschulz_passives:C-EUC0603 -> bschulz_passives:C-EU47PFC0402
- C41: device bschulz_passives:C-EUC0402 -> bschulz_passives:C-EU47PFC0402
- D1, D10, D15: value LED0603 -> LEDRED0603; device bschulz:LED0603 -> bschulz:LEDRED0603
- D11, D13, D4, D8: value LED0603 -> LEDGREEN0603; device bschulz:LED0603 -> bschulz:LEDGREEN0603
- D12, D14, D5, D9: value LED0603 -> LEDAMBER0603; device bschulz:LED0603 -> bschulz:LEDAMBER0603
- D2: DIGIKEY (none) -> 641-1747-1-ND; MF (none) -> Comchip; MPN (none) -> CDBA3100-HF
- D7: DIGIKEY (none) -> BAT54WS-TPCT-ND; MF (none) -> Micro Commercial; MPN (none) -> BAT54WS-TP
- J5: DIGIKEY (none) -> A115904CT-ND; MF (none) -> TE; MPN (none) -> 2199230-4
- L1: value 1uF -> 1uH; DIGIKEY (none) -> 732-11737-1-ND; MF (none) -> Wurth; MPN (none) -> 78438357010
- L2: DIGIKEY (none) -> 732-744383560047HTCT-ND; MF (none) -> Wurth; MPN (none) -> 744383560047HT
- L3: DIGIKEY (none) -> 732-11737-1-ND; MF (none) -> Wurth; MPN (none) -> 78438357010
- R10, R23: device bschulz_passives:R-EU_R0805 -> bschulz_passives:R-EU_0.002R0805
- R18: device bschulz_passives:R-EU_R0402 -> bschulz_passives:R-EU_20KR0402
- R21: device bschulz_passives:R-EU_R0402 -> bschulz_passives:R-EU_2.7KR0402
- R25: device bschulz_passives:R-EU_R0603 -> bschulz_passives:R-EU_470R0402
- R26: device bschulz_passives:R-EU_R0603 -> bschulz_passives:R-EU_220R0402
- R36: value (none) -> 150k; device bschulz_passives:R-EU_R0603 -> bschulz_passives:R-EU_150KR0603
- R37: value (none) -> 10k; device bschulz_passives:R-EU_R0603 -> bschulz_passives:R-EU_10KR0603
- R39: value (none) -> 130k; device bschulz_passives:R-EU_R0603 -> bschulz_passives:R-EU_130KR0603
- R40: value (none) -> 30k; device bschulz_passives:R-EU_R0603 -> bschulz_passives:R-EU_30KR0603
- R44: device bschulz_passives:R-EU_R0402 -> bschulz_passives:R-EU_10R0402
- renumbered $3_178_$_2021-10-08_21-38-43 to J5
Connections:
- new net D+_IN: D16.D+, R63.2, USB1.D+
- new net D-_IN: D16.D-, R64.2, USB1.D-
- net D+: now also R63.1; no longer USB1.D+
- net D-: now also R64.1; no longer USB1.D-
- net GND: now also D16.GND, TP1.P$1
- net OB_INT: now also TP7.P$1
- net RTC_INT: now also TP2.P$1
- net RX: now also TP9.P$1
- net SCL: now also TP6.P$1
- net SCL_OB: now also TP4.P$1
- net SDA: now also TP5.P$1
- net SDA_OB: now also TP3.P$1
- net TX: now also TP8.P$1
- net VUSB: now also D16.VBUS
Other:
- note added: "ADR: 0x20"
- note added: "ADR: 0x21"
- note removed: "ADR: 0x20 ~ 0x27"
